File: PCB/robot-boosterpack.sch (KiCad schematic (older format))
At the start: 46 parts

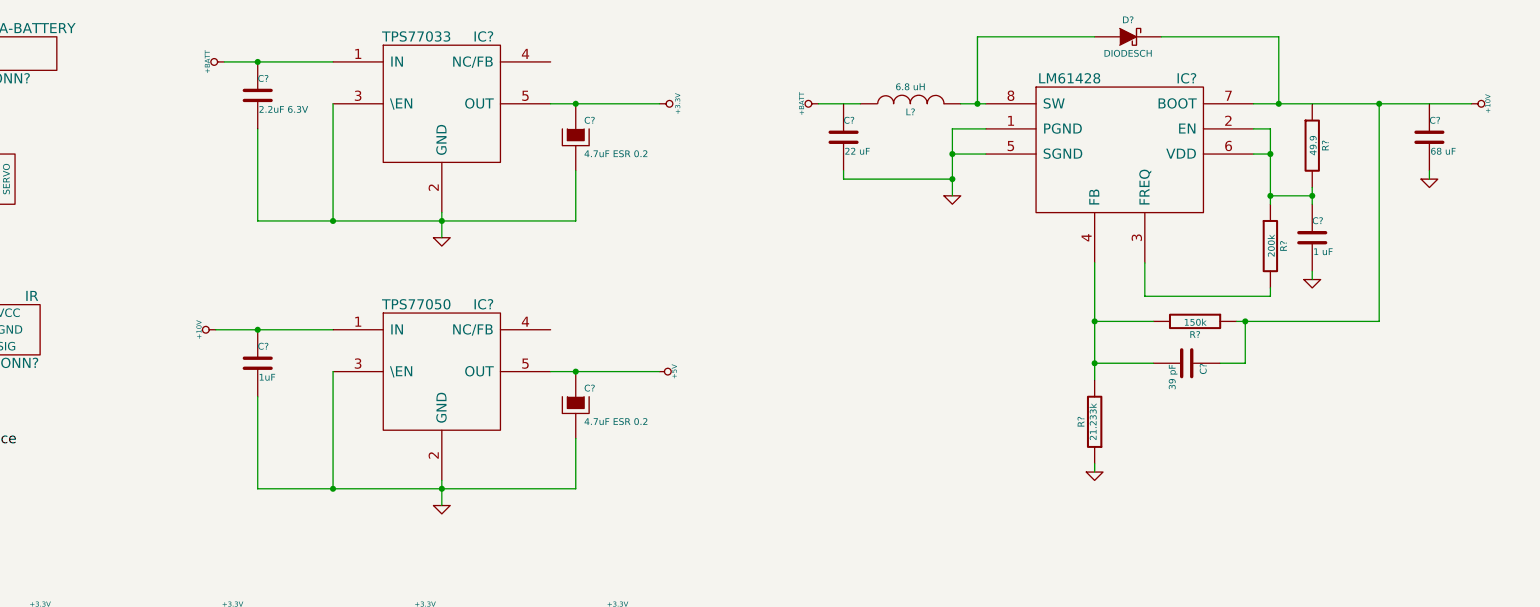
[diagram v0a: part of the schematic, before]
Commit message: added regulator jumpers
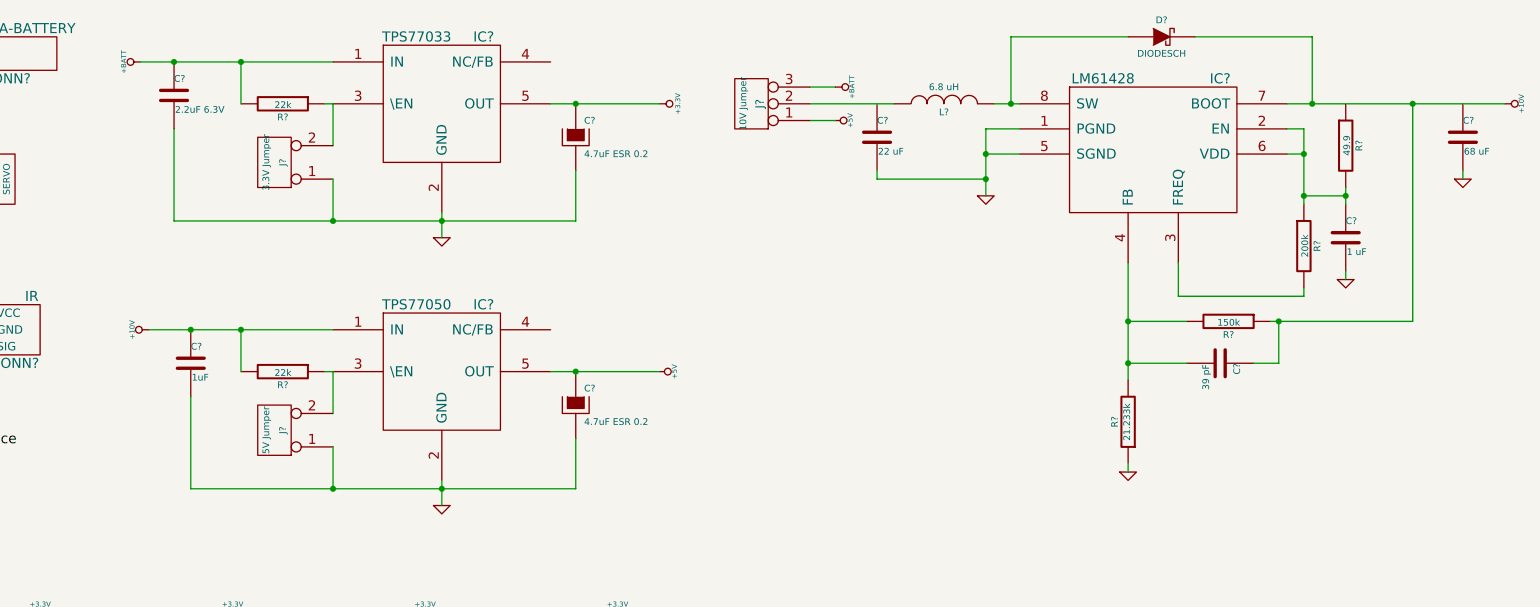
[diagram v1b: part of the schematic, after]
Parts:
- added J?: 10V Jumper, symbol CONN_3
- added J?: 3.3V Jumper, symbol CONN_2
- added J?: 5V Jumper, symbol CONN_2
- added R? (x2): 22k, ~, symbol R
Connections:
- net +10V: now also R?.2
- net +5V: now also J?.1 (P1)
- net +BATT: now also J?.3 (P3), R?.2; no longer L?.1
- net GND: now also J?.1 (P1), J?.1 (P1); no longer IC?.3 (\EN), IC?.3 (\EN)
- new net: IC?.3 (\EN), J?.2 (PM), R?.1 (x2)
- new net: J?.2 (PM), L?.1
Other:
- moved on the sheet: C?, D?, IC?, L?, R?

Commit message: annotated schematic
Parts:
- gave numbers to parts that had none: 51
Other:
- moved on the sheet: CONN3, R2, R3

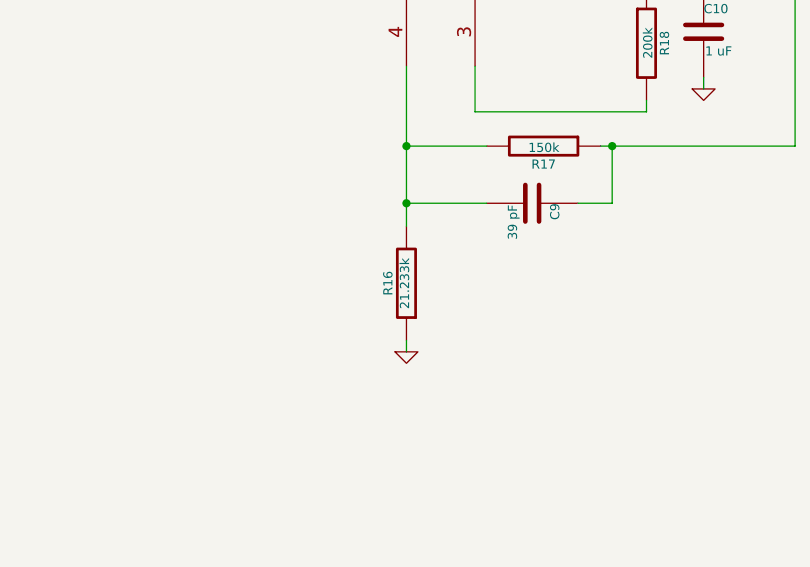
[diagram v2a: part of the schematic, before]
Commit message: changed output voltage of switching regulator to 9V from 10V
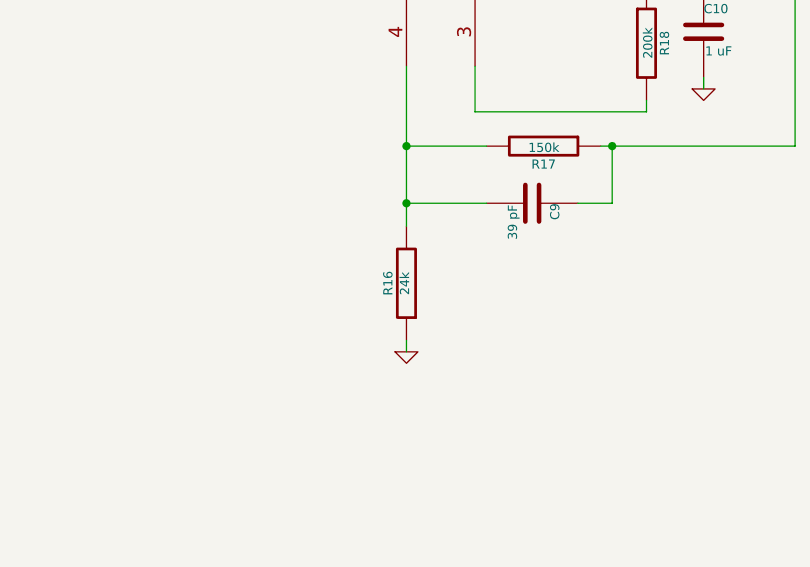
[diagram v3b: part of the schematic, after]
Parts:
- R16: value 21.233k -> 24k
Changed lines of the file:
@@
 P 8800 3050
 F 0 "R16" V 8880 3050 40  0000 C CNN
-F 1 "21.233k" V 8807 3051 40  0000 C CNN
+F 1 "24k" V 8807 3051 40  0000 C CNN
 F 2 "~" V 8730 3050 30  0000 C CNN
 F 3 "~" H 8800 3050 30  0000 C CNN

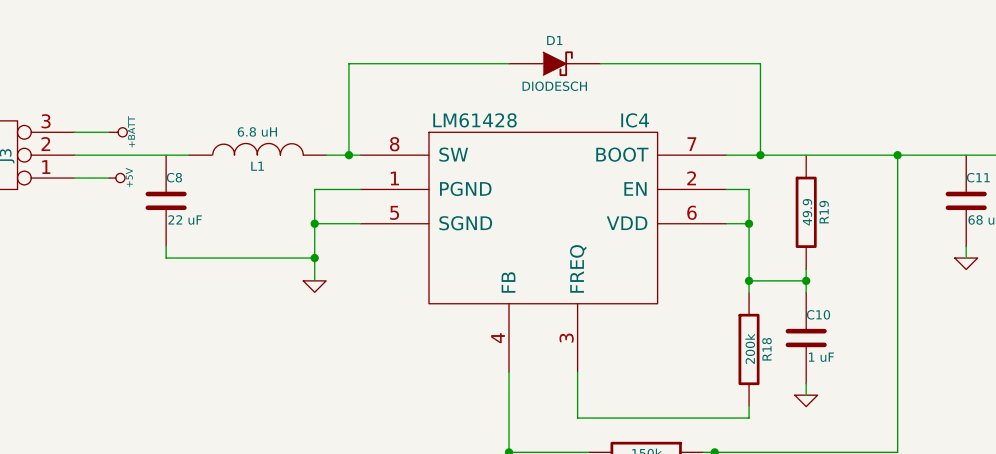
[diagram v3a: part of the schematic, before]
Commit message: changed switching regulator from bootstrap to non-bootstrapping mode
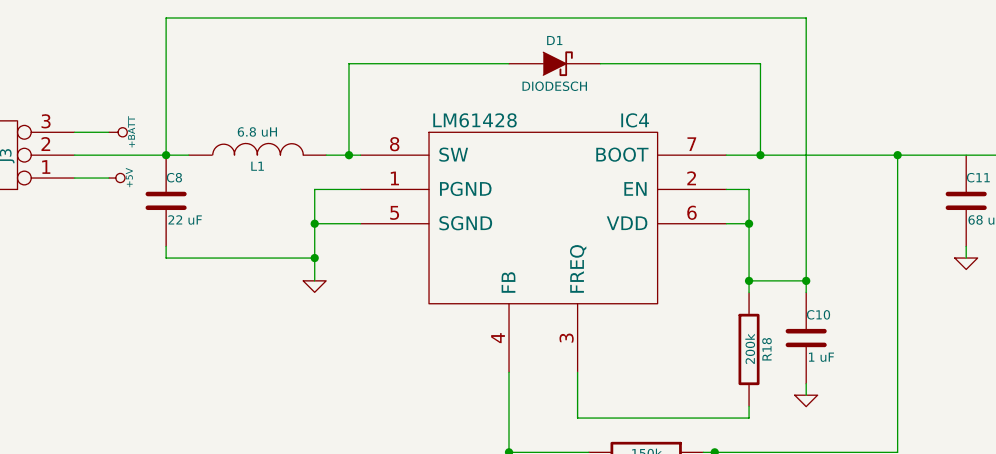
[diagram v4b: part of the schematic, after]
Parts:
- removed R19: 49.9, ~, symbol R
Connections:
- net at C10.1, IC4.2 (EN), IC4.6 (VDD)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: now also C8.1, J3.2 (PM), L1.1
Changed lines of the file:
@@
-$EndComp
-$Comp
-L R R19
-U 1 1 53A8D954
-P 10100 1400
-F 0 "R19" V 10180 1400 40  0000 C CNN
-F 1 "49.9" V 10107 1401 40  0000 C CNN
-F 2 "~" V 10030 1400 30  0000 C CNN
-F 3 "~" H 10100 1400 30  0000 C CNN
-	1    10100 1400
-	1    0    0    -1
 $EndComp
 $Comp
@@
 	9850 1700 10100 1700
 Wire Wire Line
-	10100 1650 10100 1750
+	10100 550  10100 1750
 Connection ~ 9850 1450
 Connection ~ 10100 1700
@@
 	4050 3200 4050 3450
 Connection ~ 4050 3450
+Wire Wire Line
+	10100 550  7300 550
+Wire Wire Line
+	7300 550  7300 1150
+Connection ~ 7300 1150
 $EndSCHEMATC

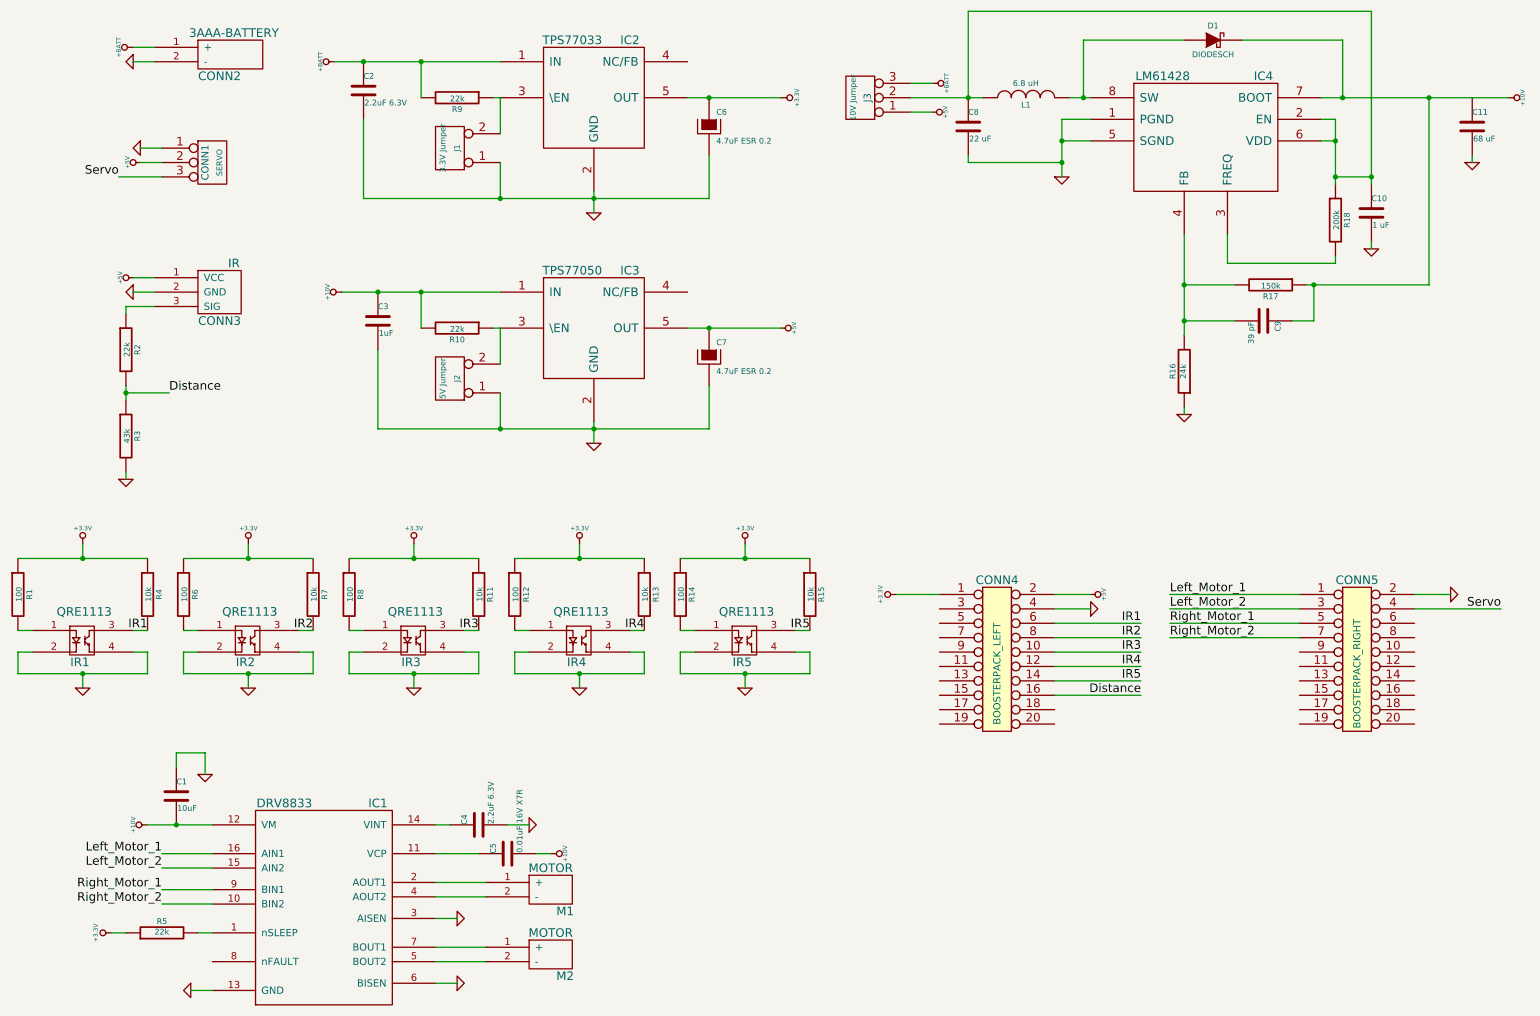
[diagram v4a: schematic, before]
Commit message: replaced 10V labels with 9V labels
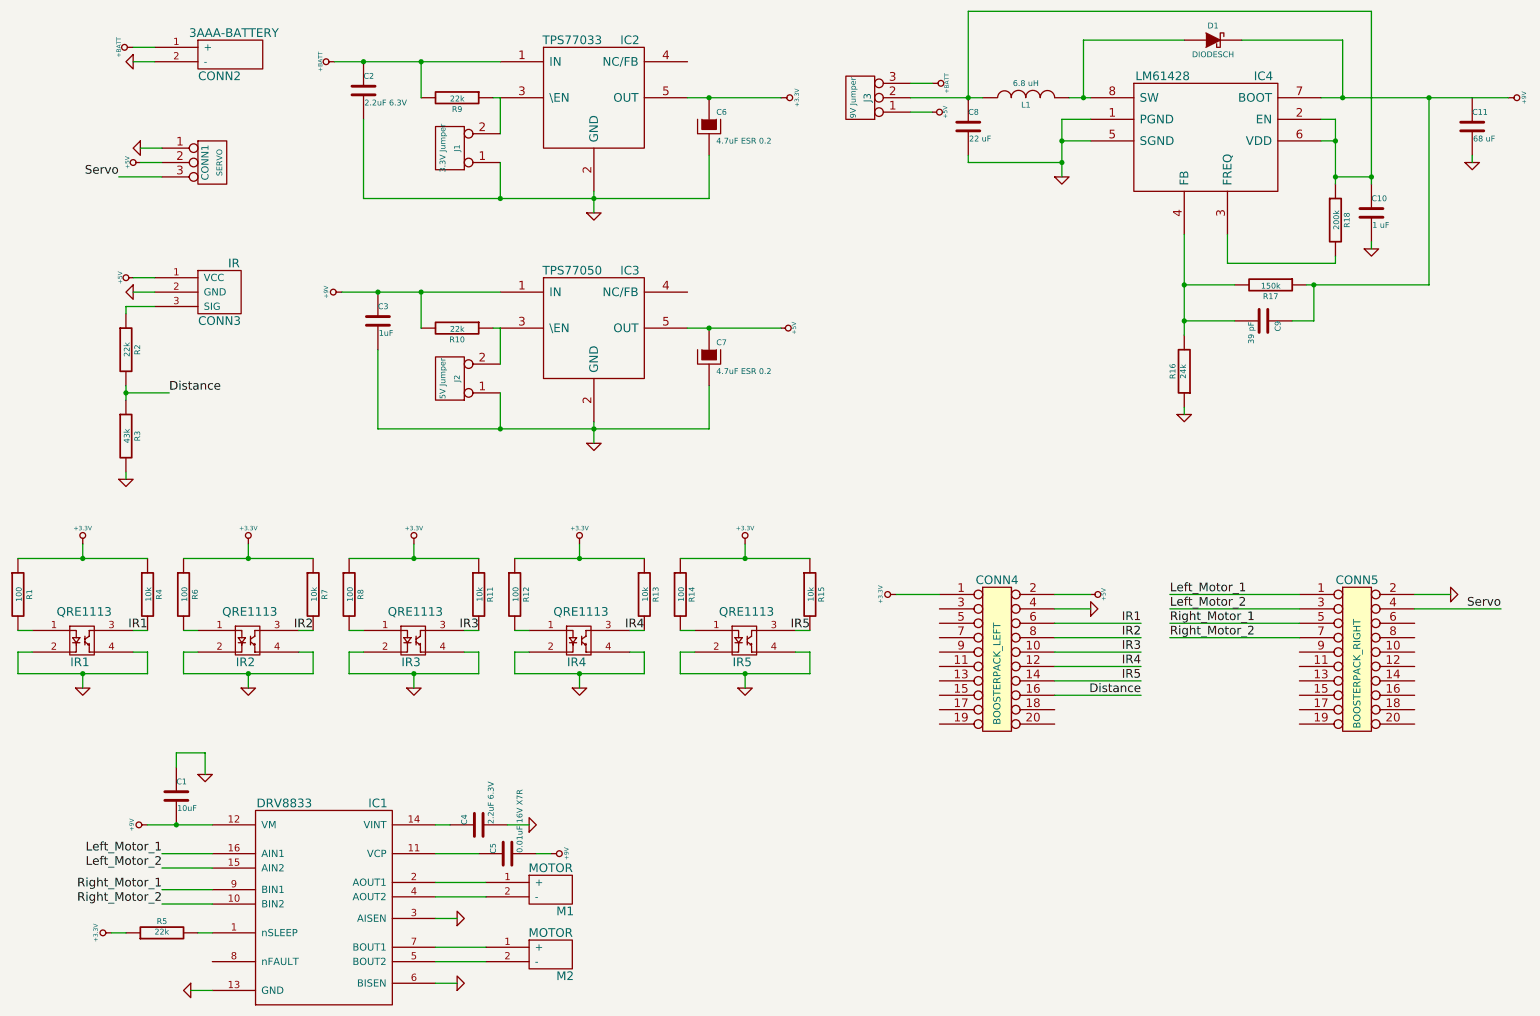
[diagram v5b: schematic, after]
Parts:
- J3: value 10V Jumper -> 9V Jumper
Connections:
- net +10V renamed +9V
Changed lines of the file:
@@
-$EndComp
-$Comp
-L +10V #PWR11
-U 1 1 53A798E9
-P 1600 6200
-F 0 "#PWR11" H 1600 6150 20  0001 C CNN
-F 1 "+10V" H 1600 6300 30  0000 C CNN
-F 2 "" H 1600 6200 60  0000 C CNN
-F 3 "" H 1600 6200 60  0000 C CNN
-	1    1600 6200
-	0    -1   -1   0
-$EndComp
-$Comp
-L +10V #PWR23
-U 1 1 53A7993E
-P 4400 6400
-F 0 "#PWR23" H 4400 6350 20  0001 C CNN
-F 1 "+10V" H 4400 6500 30  0000 C CNN
-F 2 "" H 4400 6400 60  0000 C CNN
-F 3 "" H 4400 6400 60  0000 C CNN
-	1    4400 6400
-	0    1    1    0
 $EndComp
 $Comp
@@
 $EndComp
 $Comp
-L +10V #PWR42
-U 1 1 53A8F7AA
-P 11050 1150
-F 0 "#PWR42" H 11050 1100 20  0001 C CNN
-F 1 "+10V" H 11050 1250 30  0000 C CNN
-F 2 "" H 11050 1150 60  0000 C CNN
-F 3 "" H 11050 1150 60  0000 C CNN
-	1    11050 1150
-	0    1    1    0
-$EndComp
-$Comp
 L TPS77050 IC3
 U 1 1 53A9EB1D
@@
 	1    8150 4600
 	0    1    1    0
-$EndComp
-$Comp
-L +10V #PWR17
-U 1 1 53AA074A
-P 2950 2500
-F 0 "#PWR17" H 2950 2450 20  0001 C CNN
-F 1 "+10V" H 2950 2600 30  0000 C CNN
-F 2 "" H 2950 2500 60  0000 C CNN
-F 3 "" H 2950 2500 60  0000 C CNN
-	1    2950 2500
-	0    -1   -1   0
 $EndComp
 $Comp
@@
 P 6550 1150
 F 0 "J3" V 6500 1150 50  0000 C CNN
-F 1 "10V Jumper" V 6600 1150 40  0000 C CNN
+F 1 "9V Jumper" V 6600 1150 40  0000 C CNN
 F 2 "" H 6550 1150 60  0000 C CNN
 F 3 "" H 6550 1150 60  0000 C CNN
@@
 	7300 550  7300 1150
 Connection ~ 7300 1150
+$Comp
+L +9V #PWR?
+U 1 1 53AB874F
+P 11050 1150
+F 0 "#PWR?" H 11050 1120 20  0001 C CNN
+F 1 "+9V" H 11050 1260 30  0000 C CNN
+F 2 "" H 11050 1150 60  0000 C CNN
+F 3 "" H 11050 1150 60  0000 C CNN
+	1    11050 1150
+	0    1    1    0
+$EndComp
+$Comp
+L +9V #PWR?
+U 1 1 53AB8BE0
+P 2950 2500
+F 0 "#PWR?" H 2950 2470 20  0001 C CNN
+F 1 "+9V" H 2950 2610 30  0000 C CNN
+F 2 "" H 2950 2500 60  0000 C CNN
+F 3 "" H 2950 2500 60  0000 C CNN
+	1    2950 2500
+	0    -1   -1   0
+$EndComp
+$Comp
+L +9V #PWR?
+U 1 1 53AB8FA2
+P 4400 6400
+F 0 "#PWR?" H 4400 6370 20  0001 C CNN
+F 1 "+9V" H 4400 6510 30  0000 C CNN
+F 2 "" H 4400 6400 60  0000 C CNN
+F 3 "" H 4400 6400 60  0000 C CNN
+	1    4400 6400
+	0    1    1    0
+$EndComp
+$Comp
+L +9V #PWR?
+U 1 1 53AB9207
+P 1600 6200
+F 0 "#PWR?" H 1600 6170 20  0001 C CNN
+F 1 "+9V" H 1600 6310 30  0000 C CNN
+F 2 "" H 1600 6200 60  0000 C CNN
+F 3 "" H 1600 6200 60  0000 C CNN
+	1    1600 6200
+	0    -1   -1   0
+$EndComp
 $EndSCHEMATC
